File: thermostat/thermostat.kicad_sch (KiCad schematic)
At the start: 13 parts, among them J1 Wall connections, J2 UART, U1 ESP32-WROVER-E, U2 TPS5430DDA, U3 TPS62203DBV

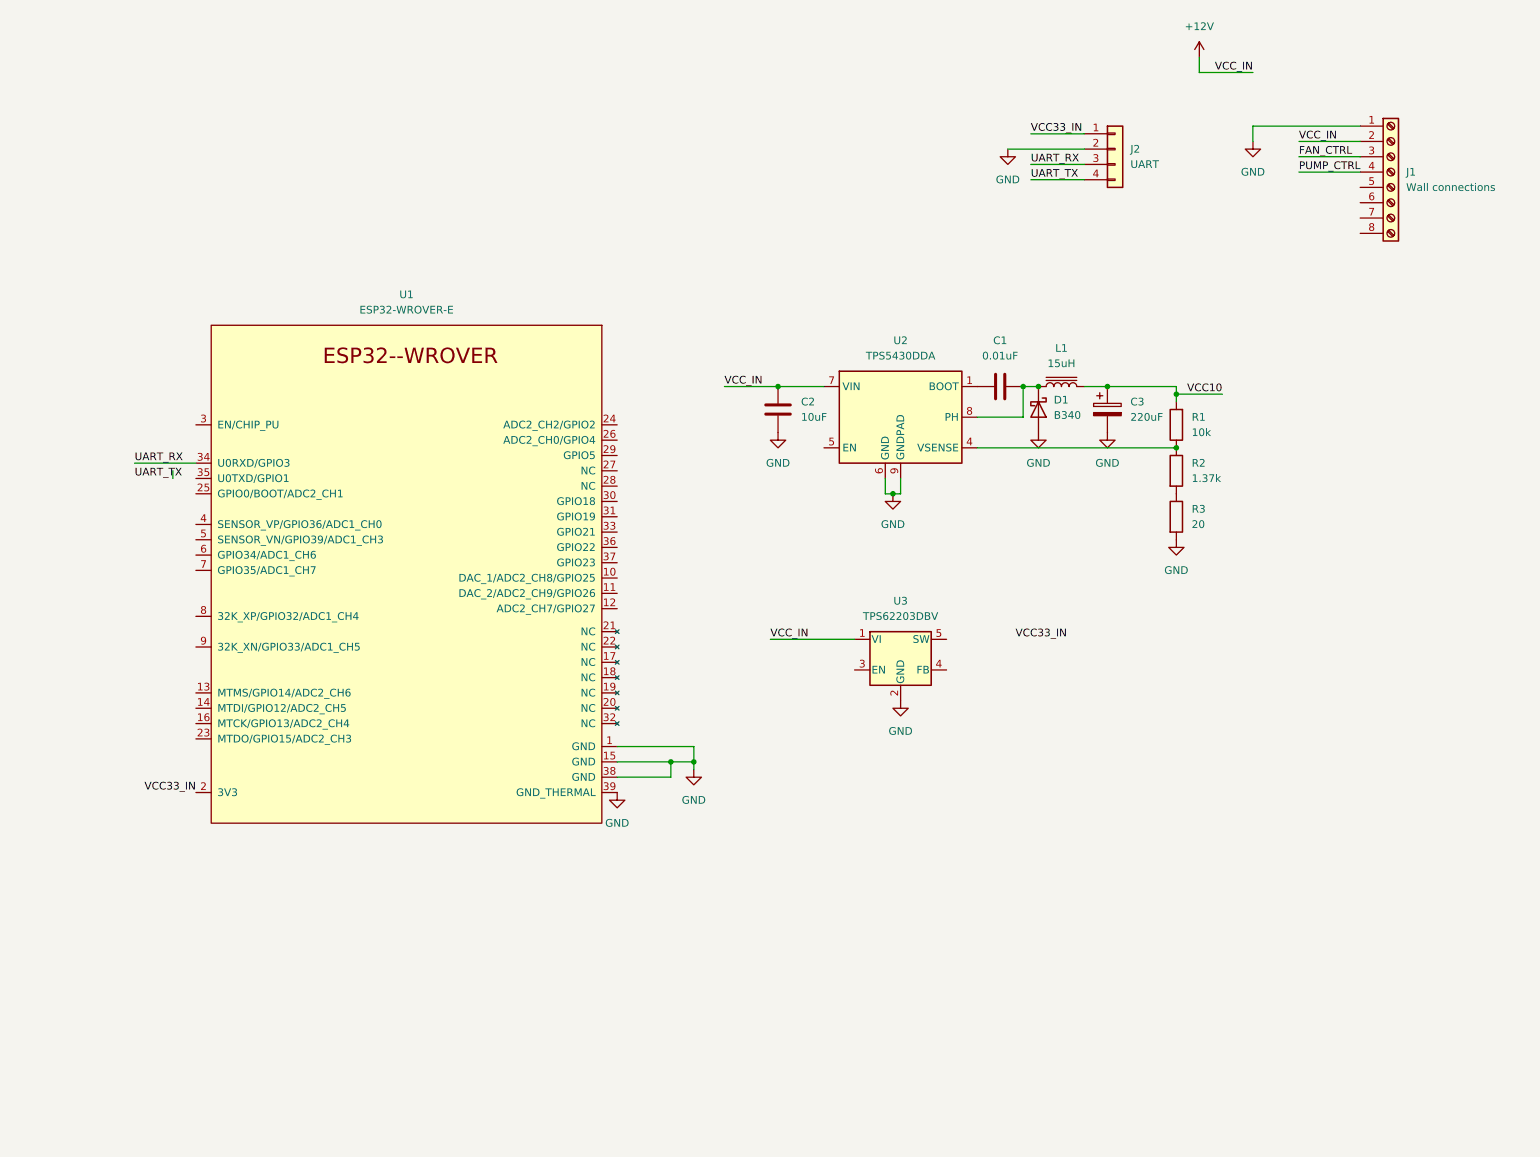
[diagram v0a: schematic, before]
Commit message: update thermostat
I think I chose all the parts, just need to optimize the layout
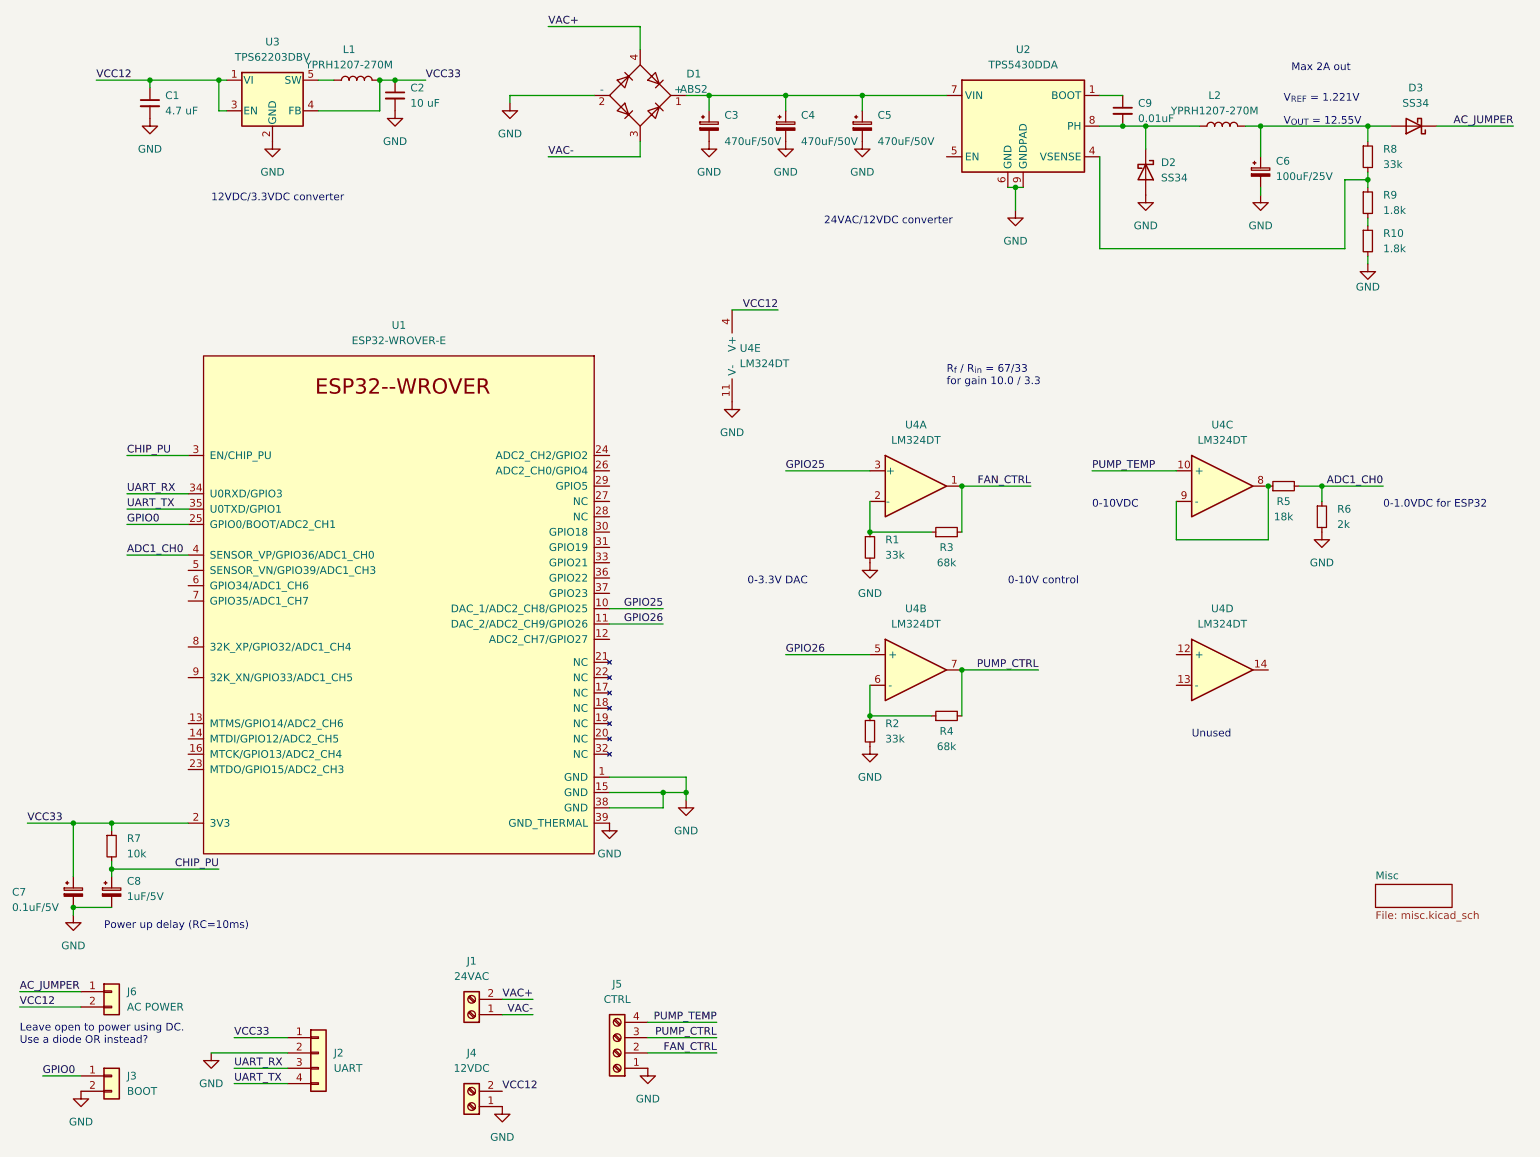
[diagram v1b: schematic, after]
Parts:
- removed C1: 0.01uF, Capacitor_SMD:C_0201_0603Metric, symbol Device:C
- removed C2: 10uF, Capacitor_SMD:C_0201_0603Metric, symbol Device:C
- removed C3: 220uF, Capacitor_SMD:C_0201_0603Metric, symbol Device:C_Polarized
- removed D1: B340, Diode_SMD:D_SMC, symbol Diode:B340
- removed J1: Wall connections, TerminalBlock_RND:TerminalBlock_RND_205-00007_1x08_P5.00mm_Horizontal, symbol Connector:Screw_Terminal_01x08
- removed L1: 15uH, Inductor_SMD:L_1210_3225Metric, symbol Device:L_Iron
- removed R1: 10k, Resistor_SMD:R_0201_0603Metric, symbol Device:R
- removed R2: 1.37k, Resistor_SMD:R_0201_0603Metric, symbol Device:R
- removed R3: 20, Resistor_SMD:R_0201_0603Metric, symbol Device:R
- added C1: 4.7 uF, Capacitor_SMD:C_0805_2012Metric, symbol Device:C_Small
- added C2: 10 uF, Capacitor_SMD:C_0805_2012Metric, symbol Device:C_Small
- added C3, C4, C5: 470uF/50V, Capacitor_SMD:CP_Elec_6.3x7.7, symbol Device:C_Polarized_Small
- added C6: 100uF/25V, Capacitor_SMD:CP_Elec_6.3x7.7, symbol Device:C_Polarized_Small
- added C7: 0.1uF/5V, symbol Device:C_Polarized_Small
- added C8: 1uF/5V, Capacitor_SMD:C_0402_1005Metric, symbol Device:C_Polarized_Small
- added C9: 0.01uF, Capacitor_SMD:C_0603_1608Metric, symbol Device:C_Small
- added D1: ABS2, Diode_SMD:Diode_Bridge_Diotec_ABS, symbol Diode_Bridge:ABS2
- added D2, D3: SS34, Diode_SMD:D_SOD-128, symbol Device:D_Schottky
- added J1: 24VAC, TerminalBlock_RND:TerminalBlock_RND_205-00001_1x02_P5.00mm_Horizontal, symbol Connector:Screw_Terminal_01x02
- added J3: BOOT, Connector_PinHeader_2.54mm:PinHeader_1x02_P2.54mm_Vertical_SMD_Pin1Left, symbol Connector_Generic:Conn_01x02
- added J4: 12VDC, TerminalBlock_RND:TerminalBlock_RND_205-00001_1x02_P5.00mm_Horizontal, symbol Connector:Screw_Terminal_01x02
- added J5: CTRL, TerminalBlock_RND:TerminalBlock_RND_205-00003_1x04_P5.00mm_Horizontal, symbol Connector:Screw_Terminal_01x04
- added J6: AC POWER, Connector_PinHeader_2.54mm:PinHeader_1x02_P2.54mm_Vertical_SMD_Pin1Left, symbol Connector_Generic:Conn_01x02
- added L1, L2: YPRH1207-270M, Inductor_SMD:L_12x12mm_H8mm, symbol Device:L
- added R1, R2, R8: 33k, Resistor_SMD:R_0201_0603Metric, symbol Device:R_Small
- added R10, R9: 1.8k, Resistor_SMD:R_0201_0603Metric, symbol Device:R_Small
- added R3, R4: 68k, Resistor_SMD:R_0201_0603Metric, symbol Device:R_Small
- added R5: 18k, Resistor_SMD:R_0201_0603Metric, symbol Device:R_Small
- added R6: 2k, Resistor_SMD:R_0201_0603Metric, symbol Device:R_Small
- added R7: 10k, Resistor_SMD:R_0201_0603Metric, symbol Device:R_Small
- added U4: LM324DT, Package_SO:SOIC-14_3.9x8.7mm_P1.27mm, symbol Device:Opamp_Quad
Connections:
- net VCC33_IN is gone; now on net VCC33: J2.1 (Pin_1), U1.2 (3V3)
- net FAN_CTRL: now also J5.2 (Pin_2), R3.2, U4.1
- net GND: now also C1.2, C2.2, C3.2, C4.2, C5.2, C6.2, C7.2, C8.2, D1.2 (-), D2.2 (A), J3.2 (Pin_2), J4.1 (Pin_1), J5.1 (Pin_1), R1.2, R10.2, R2.2, R6.2, U4.11 (V-)
- net PUMP_CTRL: now also J5.3 (Pin_3), R4.2, U4.7
- net UART_TX: now also U1.35 (U0TXD/GPIO1)
- net at U2.1 (BOOT): now also C9.1
- net at U2.8 (PH): now also C9.2, D2.1 (K), L2.1
- net GPIO25: now reaches U1.10 (DAC_1/ADC2_CH8/GPIO25)
- net GPIO25: now also U4.3 (+)
- net GPIO26: now reaches U1.11 (DAC_2/ADC2_CH9/GPIO26)
- net GPIO26: now also U4.5 (+)
- net GPIO0: now reaches U1.25 (GPIO0/BOOT/ADC2_CH1)
- net GPIO0: now also J3.1 (Pin_1)
- net CHIP_PU: now reaches U1.3 (EN/CHIP_PU)
- net CHIP_PU: now also C8.1, R7.2
- net ADC1_CH0: now reaches U1.4 (SENSOR_VP/GPIO36/ADC1_CH0)
- net ADC1_CH0: now also R5.2, R6.1
- net at U2.4 (VSENSE): now also R8.2, R9.1
- net VCC12: now reaches U3.3 (EN)
- net VCC12: now also U3.1 (VI), C1.1, J4.2 (Pin_2), J6.2 (Pin_2), U4.4 (V+)
- net VCC33: now reaches U3.4 (FB)
- net VCC33: now also C2.1, C7.1, L1.2, R7.1
- net at U3.5 (SW): now also L1.1
- net +12V: no longer names the net of U2.7 (VIN)
- net +12V: now also C3.1, C4.1, C5.1, D1.1 (+); no longer U3.1 (VI)
- new net: C6.1, D3.2 (A), L2.2, R8.1
- new net: R2.1, R4.1, U4.6 (-)
- new net: R5.1, U4.8, U4.9 (-)
- new net: R1.1, R3.1, U4.2 (-)
- new net: R10.1, R9.2
- new net AC_JUMPER: D3.1 (K), J6.1 (Pin_1)
- new net PUMP_TEMP: J5.4 (Pin_4), U4.10 (+)
- new net VAC+: D1.4, J1.2 (Pin_2)
- new net VAC-: D1.3, J1.1 (Pin_1)
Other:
- added sheet Misc (misc.kicad_sch)
- note added: "0-1.0VDC for ESP32"
- note added: "0-10V control"
- note added: "0-10VDC"
- note added: "0-3.3V DAC"
- note added: "12VDC/3.3VDC converter"
- note added: "24VAC/12VDC converter"
- note added: "Leave open to power using DC. Use a diode OR instead?"
- note added: "Max 2A out"
- note added: "Power up delay (RC=10ms)"
- note added: "R_{f} / R_{in} = 67/33 for gain 10.0 / 3.3"
- note added: "Unused"
- note added: "V_{OUT} = 12.55V"
- note added: "V_{REF} = 1.221V"
- moved on the sheet: J2, U1, U3

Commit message: layout with holes to fit in old slot
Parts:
- removed J6: AC POWER, Connector_PinHeader_2.54mm:PinHeader_1x02_P2.54mm_Vertical_SMD_Pin1Left, symbol Connector_Generic:Conn_01x02
- C7: footprint (none) -> Capacitor_SMD:C_0201_0603Metric
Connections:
- net AC_JUMPER is gone; now on net VCC12: D3.1 (K)
- net GPIO25 renamed DAC_1
- net GPIO26 renamed DAC_2
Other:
- note added: "IN: 0-3.3VDC"
- note added: "Max 3A out"
- note added: "OUT: 0-10VDC"
- note added: "Pick terminal blocks"
- note removed: "0-10V control"
- note removed: "0-3.3V DAC"
- note removed: "Leave open to power using DC. Use a diode OR instead?"
- note removed: "Max 2A out"
- moved on the sheet: J3
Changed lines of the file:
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@@
-    (stroke (width 0) (type default) (color 0 0 0 0))
-  )
-  (wire (pts (xy 15.24 176.53) (xy 25.4 176.53))
     (stroke (width 0) (type default) (color 0 0 0 0))
   )
@@
     (stroke (width 0) (type default) (color 0 0 0 0))
   )
-  (wire (pts (xy 15.24 179.07) (xy 25.4 179.07))
-    (stroke (width 0) (type default) (color 0 0 0 0))
-  )
   (wire (pts (xy 102.87 38.1) (xy 118.11 38.1))
     (stroke (width 0) (type default) (color 0 0 0 0))
@@
     (stroke (width 0) (type default) (color 0 0 0 0))
   )
-  (wire (pts (xy 19.05 190.5) (xy 25.4 190.5))
+  (wire (pts (xy 19.05 186.69) (xy 25.4 186.69))
     (stroke (width 0) (type default) (color 0 0 0 0))
   )
@@
     (effects (font (size 1.27 1.27)) (justify left bottom))
   )
-  (text "0-10V control" (at 179.07 109.22 0)
+  (text "OUT: 0-10VDC" (at 172.72 111.76 0)
     (effects (font (size 1.27 1.27)) (justify left bottom))
   )
@@
     (effects (font (size 1.27 1.27)) (justify left bottom))
   )
+  (text "Pick terminal blocks" (at 106.68 199.39 0)
+    (effects (font (size 1.27 1.27)) (justify left bottom))
+  )
   (text "R_{f} / R_{in} = 67/33\nfor gain 10.0 / 3.3" (at 168.91 76.2 0)
     (effects (font (size 1.27 1.27)) (justify left bottom))
   )
-  (text "Max 2A out" (at 226.06 24.13 0)
+  (text "Max 3A out" (at 226.06 24.13 0)
     (effects (font (size 1.27 1.27)) (justify left bottom))
   )
@@
     (effects (font (size 1.27 1.27)) (justify left bottom))
   )
-  (text "0-3.3V DAC" (at 135.89 109.22 0)
+  (text "IN: 0-3.3VDC" (at 137.16 111.76 0)
     (effects (font (size 1.27 1.27)) (justify left bottom))
   )
@@
     (effects (font (size 1.27 1.27)) (justify left bottom))
   )
-  (text "Leave open to power using DC.\nUse a diode OR instead?"
-    (at 15.24 185.42 0)
-    (effects (font (size 1.27 1.27)) (justify left bottom))
-  )
   (text "0-10VDC" (at 193.04 96.52 0)
     (effects (font (size 1.27 1.27)) (justify left bottom))
   )
   (text "12VDC/3.3VDC converter" (at 46.99 45.72 0)
-    (effects (font (size 1.27 1.27)) (justify left bottom))
-  )
-  (label "VCC12" (at 15.24 179.07 0)
     (effects (font (size 1.27 1.27)) (justify left bottom))
   )
@@
     (effects (font (size 1.27 1.27)) (justify left bottom))
   )
-  (label "GPIO0" (at 19.05 190.5 0)
+  (label "GPIO0" (at 19.05 186.69 0)
     (effects (font (size 1.27 1.27)) (justify left bottom))
   )
@@
     (effects (font (size 1.27 1.27)) (justify left bottom))
   )
-  (label "GPIO25" (at 142.24 90.17 0)
+  (label "DAC_1" (at 142.24 90.17 0)
     (effects (font (size 1.27 1.27)) (justify left bottom))
   )
@@
     (effects (font (size 1.27 1.27)) (justify left bottom))
   )
-  (label "AC_JUMPER" (at 262.89 33.02 180)
+  (label "VCC12" (at 262.89 33.02 180)
     (effects (font (size 1.27 1.27)) (justify right bottom))
   )
-  (label "AC_JUMPER" (at 15.24 176.53 0)
-    (effects (font (size 1.27 1.27)) (justify left bottom))
-  )
-  (label "GPIO26" (at 142.24 120.65 0)
+  (label "DAC_2" (at 142.24 120.65 0)
     (effects (font (size 1.27 1.27)) (justify left bottom))
   )
@@
     (effects (font (size 1.27 1.27)) (justify left bottom))
   )
-  (label "GPIO26" (at 121.92 115.57 180)
+  (label "DAC_2" (at 121.92 115.57 180)
     (effects (font (size 1.27 1.27)) (justify right bottom))
   )
@@
     (effects (font (size 1.27 1.27)) (justify right bottom))
   )
-  (label "GPIO25" (at 121.92 113.03 180)
+  (label "DAC_1" (at 121.92 113.03 180)
     (effects (font (size 1.27 1.27)) (justify right bottom))
   )
@@
       (effects (font (size 1.27 1.27)) (justify left))
     )
-    (property "Footprint" "" (id 2) (at 24.13 160.02 0)
+    (property "Footprint" "Capacitor_SMD:C_0201_0603Metric" (id 2) (at 24.13 160.02 0)
       (effects (font (size 1.27 1.27)) hide)
     )
@@
     )
     (pin "1")
-  )
-  (symbol (lib_id "Connector_Generic:Conn_01x02") (at 30.48 176.53 0) (unit 1)
-    (in_bom yes) (on_board yes) (fields_autoplaced)
-    (property "Reference" "J6" (id 0) (at 33.02 176.5299 0)
-      (effects (font (size 1.27 1.27)) (justify left))
-    )
-    (property "Value" "AC POWER" (id 1) (at 33.02 179.0699 0)
-      (effects (font (size 1.27 1.27)) (justify left))
-    )
-    (property "Footprint" "Connector_PinHeader_2.54mm:PinHeader_1x02_P2.54mm_Vertical_SMD_Pin1Left" (id 2) (at 30.48 176.53 0)
-      (effects (font (size 1.27 1.27)) hide)
-    )
-    (property "Datasheet" "~" (id 3) (at 30.48 176.53 0)
-      (effects (font (size 1.27 1.27)) hide)
-    )
-    (pin "1")
-    (pin "2")
   )
   (symbol (lib_id "Device:R_Small") (at 30.48 152.4 0) (unit 1)
@@
     (pin "4")
   )
-  (symbol (lib_id "power:GND") (at 25.4 193.04 0) (unit 1)
-    (in_bom yes) (on_board yes) (fields_autoplaced)
-    (property "Reference" "#PWR0101" (id 0) (at 25.4 199.39 0)
-      (effects (font (size 1.27 1.27)) hide)
-    )
-    (property "Value" "GND" (id 1) (at 25.4 198.12 0))
-    (property "Footprint" "" (id 2) (at 25.4 193.04 0)
-      (effects (font (size 1.27 1.27)) hide)
-    )
-    (property "Datasheet" "" (id 3) (at 25.4 193.04 0)
+  (symbol (lib_id "power:GND") (at 25.4 189.23 0) (unit 1)
+    (in_bom yes) (on_board yes) (fields_autoplaced)
+    (property "Reference" "#PWR0101" (id 0) (at 25.4 195.58 0)
+      (effects (font (size 1.27 1.27)) hide)
+    )
+    (property "Value" "GND" (id 1) (at 25.4 194.31 0))
+    (property "Footprint" "" (id 2) (at 25.4 189.23 0)
+      (effects (font (size 1.27 1.27)) hide)
+    )
+    (property "Datasheet" "" (id 3) (at 25.4 189.23 0)
       (effects (font (size 1.27 1.27)) hide)
     )
@@
     (pin "2")
   )
-  (symbol (lib_id "Connector_Generic:Conn_01x02") (at 30.48 190.5 0) (unit 1)
-    (in_bom yes) (on_board yes) (fields_autoplaced)
-    (property "Reference" "J3" (id 0) (at 33.02 190.4999 0)
-      (effects (font (size 1.27 1.27)) (justify left))
-    )
-    (property "Value" "BOOT" (id 1) (at 33.02 193.0399 0)
-      (effects (font (size 1.27 1.27)) (justify left))
-    )
-    (property "Footprint" "Connector_PinHeader_2.54mm:PinHeader_1x02_P2.54mm_Vertical_SMD_Pin1Left" (id 2) (at 30.48 190.5 0)
-      (effects (font (size 1.27 1.27)) hide)
-    )
-    (property "Datasheet" "~" (id 3) (at 30.48 190.5 0)
+  (symbol (lib_id "Connector_Generic:Conn_01x02") (at 30.48 186.69 0) (unit 1)
+    (in_bom yes) (on_board yes) (fields_autoplaced)
+    (property "Reference" "J3" (id 0) (at 33.02 186.6899 0)
+      (effects (font (size 1.27 1.27)) (justify left))
+    )
+    (property "Value" "BOOT" (id 1) (at 33.02 189.2299 0)
+      (effects (font (size 1.27 1.27)) (justify left))
+    )
+    (property "Footprint" "Connector_PinHeader_2.54mm:PinHeader_1x02_P2.54mm_Vertical_SMD_Pin1Left" (id 2) (at 30.48 186.69 0)
+      (effects (font (size 1.27 1.27)) hide)
+    )
+    (property "Datasheet" "~" (id 3) (at 30.48 186.69 0)
       (effects (font (size 1.27 1.27)) hide)
     )
@@
     )
     (path "/faaee792-4833-428a-83e0-e73465964898/25d143e0-4df7-490d-9b34-dae4a8cc9d87"
-      (reference "H1") (unit 1) (value "MountingHole_Pad") (footprint "MountingHole:MountingHole_2.2mm_M2_DIN965_Pad_TopBottom")
+      (reference "H1") (unit 1) (value "MountingHole_Pad") (footprint "kelvie:MountingHole_No6_Pad_TopBottom")
     )
     (path "/faaee792-4833-428a-83e0-e73465964898/3ed0d3fb-2605-4544-868d-f334e0000acc"
-      (reference "H2") (unit 1) (value "MountingHole_Pad") (footprint "MountingHole:MountingHole_2.2mm_M2_DIN965_Pad_TopBottom")
+      (reference "H2") (unit 1) (value "MountingHole_Pad") (footprint "kelvie:MountingHole_No6_Pad_TopBottom")
     )
     (path "/faaee792-4833-428a-83e0-e73465964898/0aaa5351-5898-4581-b2a8-3e3192f6b096"
@@
       (reference "J5") (unit 1) (value "CTRL") (footprint "TerminalBlock_RND:TerminalBlock_RND_205-00003_1x04_P5.00mm_Horizontal")
     )
-    (path "/220b4f3d-3762-4b86-8f84-3b146a22654a"
-      (reference "J6") (unit 1) (value "AC POWER") (footprint "Connector_PinHeader_2.54mm:PinHeader_1x02_P2.54mm_Vertical_SMD_Pin1Left")
-    )
     (path "/9ba95564-4754-4706-856d-4afe4599e848"

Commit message: Better layout with shorter debug pins
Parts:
- J2: footprint Connector_PinHeader_2.54mm:PinHeader_1x04_P2.54mm_Vertical_SMD_Pin1Left -> Connector_PinHeader_2.54mm:PinHeader_1x04_P2.54mm_Horizontal
- J3: footprint Connector_PinHeader_2.54mm:PinHeader_1x02_P2.54mm_Vertical_SMD_Pin1Left -> Connector_PinHeader_2.54mm:PinHeader_1x02_P2.54mm_Horizontal
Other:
- note added: "TODO: Pick terminal blocks"
- note removed: "Pick terminal blocks"
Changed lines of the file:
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@@
     (effects (font (size 1.27 1.27)) (justify left bottom))
   )
-  (text "Pick terminal blocks" (at 106.68 199.39 0)
+  (text "TODO: Pick terminal blocks" (at 106.68 199.39 0)
     (effects (font (size 1.27 1.27)) (justify left bottom))
   )
@@
       (effects (font (size 1.27 1.27)) (justify left))
     )
-    (property "Footprint" "Connector_PinHeader_2.54mm:PinHeader_1x04_P2.54mm_Vertical_SMD_Pin1Left" (id 2) (at 64.77 186.69 0)
+    (property "Footprint" "Connector_PinHeader_2.54mm:PinHeader_1x04_P2.54mm_Horizontal" (id 2) (at 64.77 186.69 0)
       (effects (font (size 1.27 1.27)) hide)
     )
@@
       (effects (font (size 1.27 1.27)) (justify left))
     )
-    (property "Footprint" "Connector_PinHeader_2.54mm:PinHeader_1x02_P2.54mm_Vertical_SMD_Pin1Left" (id 2) (at 30.48 186.69 0)
+    (property "Footprint" "Connector_PinHeader_2.54mm:PinHeader_1x02_P2.54mm_Horizontal" (id 2) (at 30.48 186.69 0)
       (effects (font (size 1.27 1.27)) hide)
     )
@@
     )
     (path "/4e95019e-b569-4f40-a915-152c56fdc6b6"
-      (reference "J2") (unit 1) (value "UART") (footprint "Connector_PinHeader_2.54mm:PinHeader_1x04_P2.54mm_Vertical_SMD_Pin1Left")
+      (reference "J2") (unit 1) (value "UART") (footprint "Connector_PinHeader_2.54mm:PinHeader_1x04_P2.54mm_Horizontal")
     )
     (path "/eb5ab455-942a-43af-a839-570a1ee4293e"
-      (reference "J3") (unit 1) (value "BOOT") (footprint "Connector_PinHeader_2.54mm:PinHeader_1x02_P2.54mm_Vertical_SMD_Pin1Left")
+      (reference "J3") (unit 1) (value "BOOT") (footprint "Connector_PinHeader_2.54mm:PinHeader_1x02_P2.54mm_Horizontal")
     )
     (path "/b20be9e5-ed14-4197-ac24-450f03e4ef9c"
